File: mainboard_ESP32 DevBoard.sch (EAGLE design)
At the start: 44 parts, among them IC1 OP-AMP-2-LONG, K1 AQH213, T1 2N2222, X1 JST-XH-02-PIN-LONG-PAD, X2 JST-XH-04-PIN-LONG-PAD, X3 1751293, X4 JST-XH-04-PIN-LONG-PAD

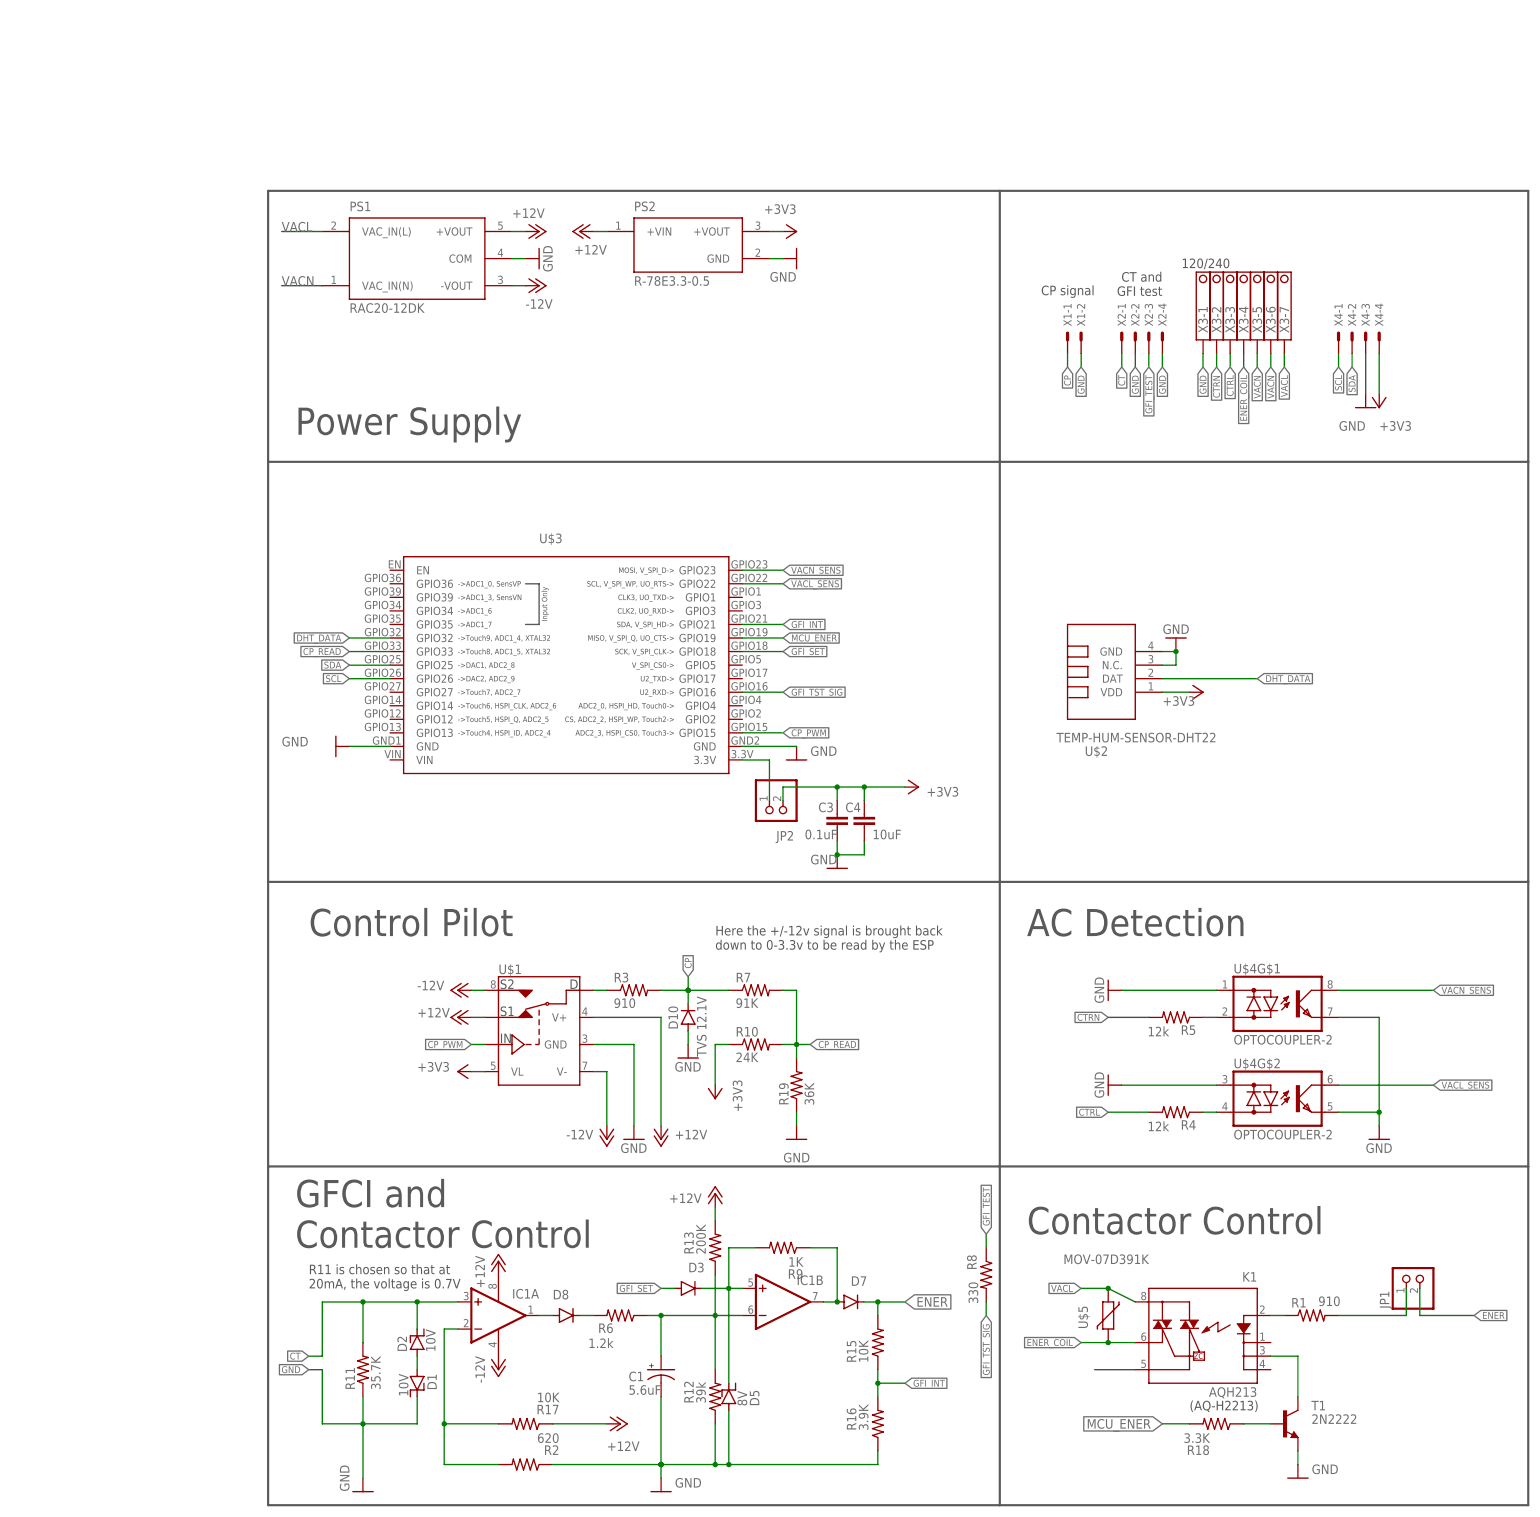
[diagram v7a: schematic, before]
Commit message: Creating the BOM on digikey uncovered some footprint mismatches. They havee been corrected
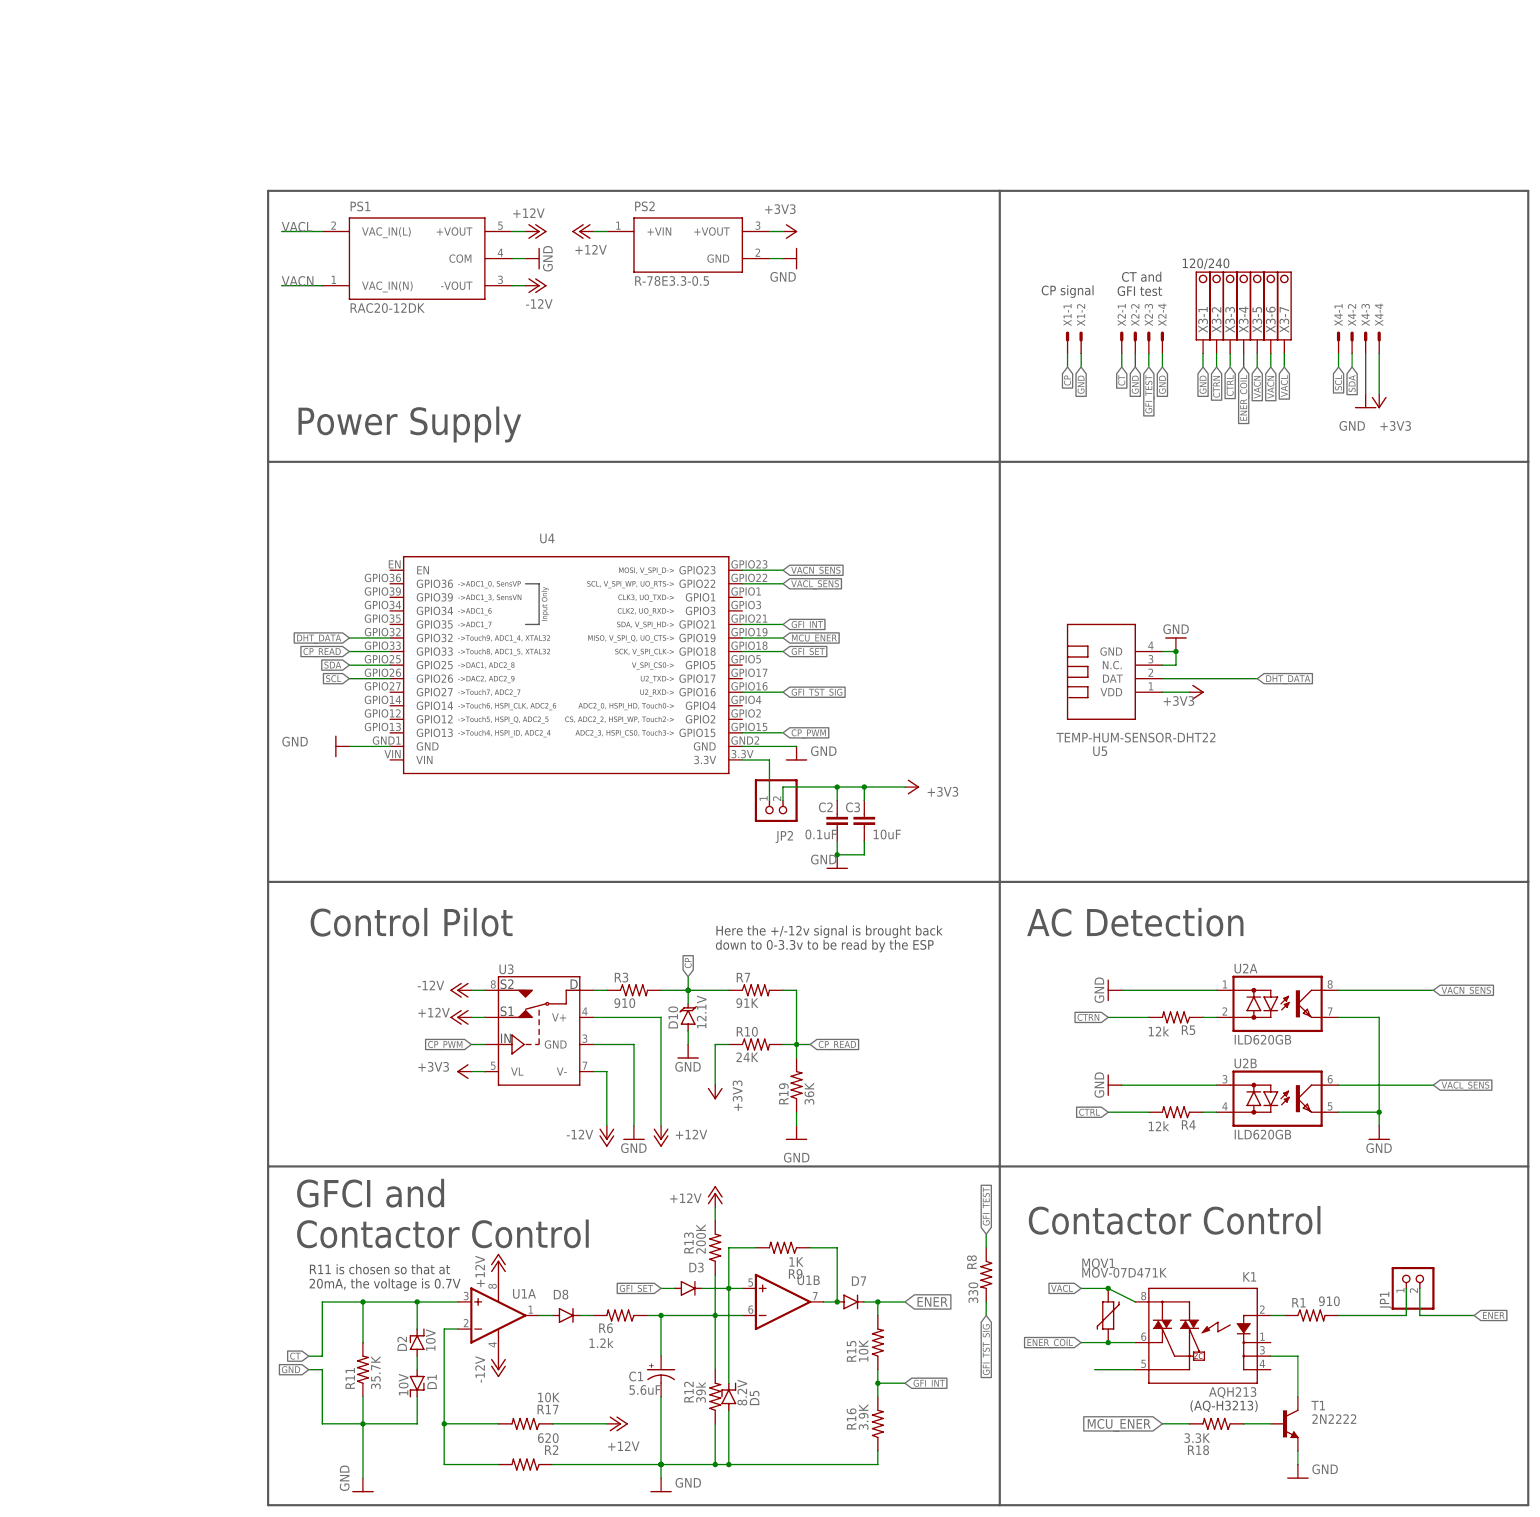
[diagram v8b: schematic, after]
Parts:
- removed C4: 10uF, rcl:C-EU025-025X050
- removed IC1: OP-AMP-2-LONG, Op Amp:OP-AMP-2-LONG
- removed U$1: DG419DJ-L, Analog Switches:DG419DJ-L
- removed U$4: OPTOCOUPLER-2, optocouplers:OPTOCOUPLER-2
- removed U$5: MOV-07D391K, EVSE:MOV-07D391K
- added C2: 0.1uF, rcl:C-EU025-025X050
- added MOV1: MOV-07D471K, EVSE:MOV-07D471K
- added U1: LM833N, EVSE:LM833N
- added U2: ILD620GB, EVSE:ILD620GB
- added U3: DG419DJ-L, EVSE:DG419DJ-L
- C3: value 0.1uF -> 10uF; device rcl:C-EU025-025X050 -> rcl:C-EU025-050X050
- D10: value TVS 12.1V -> 12.1V; device Passive:DIODE -> EVSE:P6KE15AL
- D5: value 8V -> 8.2V
- PS1: device RAC20-12DK:RAC20-12DK -> EVSE:RAC20-12DK
- PS2: device R-78E3.3-0.5:R-78E3.3-0.5 -> EVSE:R-78E3.3-0.5
- renumbered U$2 to U5, U$3 to U4
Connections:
- net +12V: now also U1P.V+, U3.S1, U3.V+; no longer IC1P.V+, U$1.S1, U$1.V+
- net +3V3: now also C2.1, U3.VL; no longer C4.1, U$1.VL
- net -12V: now also U1P.V-, U3.S2, U3.V-; no longer IC1P.V-, U$1.S2, U$1.V-
- net CP_PWM: now also U3.IN; no longer U$1.IN
- net CT: now also U1A.+IN; no longer IC1A.+IN
- net ENER_COIL: now also MOV1.2; no longer U$5.2
- net GND: now also C2.2, U2A.AC1, U2A.E, U2B.AC1, U2B.E, U3.GND; no longer C4.2, U$1.GND, U$4G$1.AC1, U$4G$1.E, U$4G$2.AC1, U$4G$2.E
- net N$13: now also U1B.+IN; no longer IC1B.+IN
- net N$15: now also U1A.OUT; no longer IC1A.OUT
- net N$16: now also U2A.AC2; no longer U$4G$1.AC2
- net N$17: now also U2B.AC2; no longer U$4G$2.AC2
- net N$2: now also U1A.-IN; no longer IC1A.-IN
- net N$4: now also U1B.OUT; no longer IC1B.OUT
- net N$8: now also U3.D; no longer U$1.D
- net N$9: now also U1B.-IN; no longer IC1B.-IN
- net VACL: now also MOV1.1; no longer U$5.1
- net VACL_SENS: now also U2B.C; no longer U$4G$2.C
- net VACN_SENS: now also U2A.C; no longer U$4G$1.C
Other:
- note added: "(AQ-H3213)"
- note removed: "(AQ-H2213)"
- moved on the sheet: C3
